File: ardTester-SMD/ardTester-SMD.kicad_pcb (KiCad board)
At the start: 2 copper layers, 143.5 x 114.3 mm, 54 parts, among them SW1 SW_DIP_x02, U1 Arduino_Mini_Pro, U2 Power In, U3 Arduino_Mini_Pro

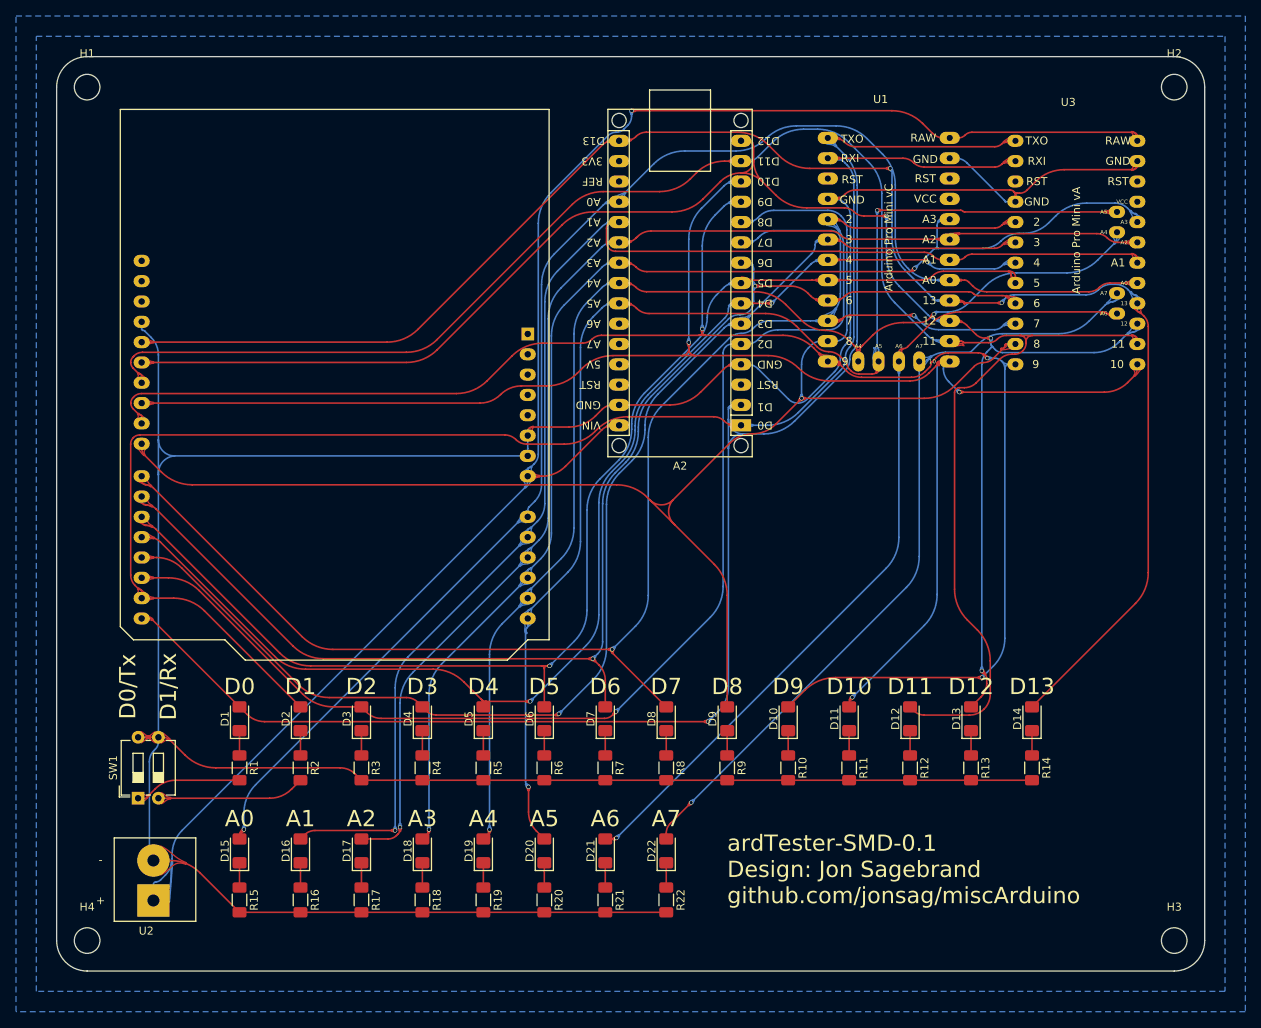
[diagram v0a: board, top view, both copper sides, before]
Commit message: atmega/arduino tester
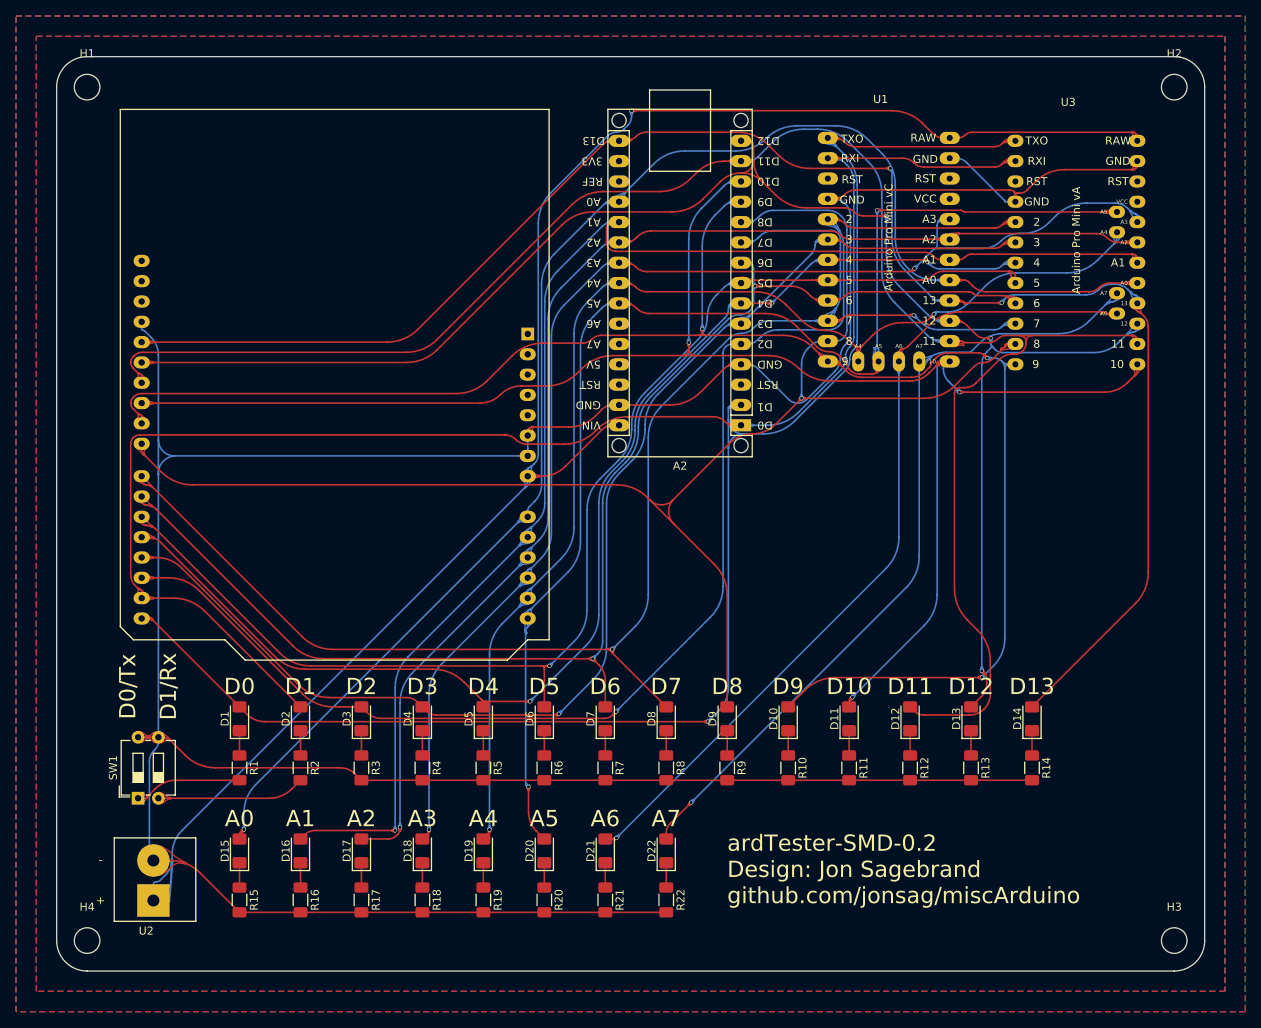
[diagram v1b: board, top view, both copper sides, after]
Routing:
- added copper zone on F.Cu, net (none)
- added copper zone on F.Cu, net GND
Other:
- board text added: "ardTester-SMD-0.2 Design: Jon Sagebrand github.com/jonsag/miscArduino"
- board text removed: "ardTester-SMD-0.1 Design: Jon Sagebrand github.com/jonsag/miscArduino"
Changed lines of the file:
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@@
     (effects (font (size 2.032 2.032) (thickness 0.254)))
   )
-  (gr_text "ardTester-SMD-0.1\nDesign: Jon Sagebrand\ngithub.com/jonsag/miscArduino" (at 162.56 132.08) (layer "F.SilkS")
+  (gr_text "ardTester-SMD-0.2\nDesign: Jon Sagebrand\ngithub.com/jonsag/miscArduino" (at 162.56 132.08) (layer "F.SilkS")
     (effects (font (size 2.032 2.032) (thickness 0.254)) (justify left))
   )
@@
     )
   )
+  (zone (net 41) (net_name "GND") (layers F&B.Cu) (hatch edge 0.508)
+    (connect_pads (clearance 0.508))
+    (min_thickness 0.254) (filled_areas_thickness no)
+    (fill yes (thermal_gap 0.508) (thermal_bridge_width 0.508))
+    (polygon
+      (pts
+        (xy 224.79 147.32)
+        (xy 76.2 147.32)
+        (xy 76.2 27.94)
+        (xy 224.79 27.94)
+      )
+    )
+  )
   (zone (net 8) (net_name "D4") (layer "F.Cu") (hatch edge 0.508)
     (priority 16962)
@@
     )
   )
+  (zone (net 0) (net_name "") (layers F&B.Cu) (hatch edge 0.508)
+    (connect_pads (clearance 0.508))
+    (min_thickness 0.254) (filled_areas_thickness no)
+    (fill yes (thermal_gap 0.508) (thermal_bridge_width 0.508))
+    (polygon
+      (pts
+        (xy 227.33 149.86)
+        (xy 73.66 149.86)
+        (xy 73.66 25.4)
+        (xy 227.33 25.4)
+      )
+    )
+  )
   (zone (net 32) (net_name "A2") (layer "F.Cu") (hatch edge 0.508)
     (priority 16962)
@@
     )
   )
-  (zone (net 41) (net_name "GND") (layer "B.Cu") (hatch edge 0.508)
-    (connect_pads (clearance 0.508))
-    (min_thickness 0.254) (filled_areas_thickness no)
-    (fill yes (thermal_gap 0.508) (thermal_bridge_width 0.508))
-    (polygon
-      (pts
-        (xy 224.79 147.32)
-        (xy 76.2 147.32)
-        (xy 76.2 27.94)
-        (xy 224.79 27.94)
-      )
-    )
-  )
   (zone (net 39) (net_name "D0") (layer "B.Cu") (hatch edge 0.508)
     (priority 16962)
@@
       )
     )
-  )
-  (zone (net 0) (net_name "") (layer "B.Cu") (hatch edge 0.508)
-    (connect_pads (clearance 0.508))
-    (min_thickness 0.254) (filled_areas_thickness no)
-    (fill yes (thermal_gap 0.508) (thermal_bridge_width 0.508))
-    (polygon
-      (pts
-        (xy 227.33 149.86)
-        (xy 73.66 149.86)
-        (xy 73.66 25.4)
-        (xy 227.33 25.4)
-      )
-    )
